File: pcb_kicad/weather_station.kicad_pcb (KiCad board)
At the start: 0 parts

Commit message: added full pcb schematic
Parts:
- added BT1: Battery_Cell, Battery:BatteryHolder_Keystone_1042_1x18650, F.Cu at (95.0, 105.1)
- added C1: 22u, Capacitor_SMD:C_0603_1608Metric_Pad1.08x0.95mm_HandSolder, F.Cu at (111.0, 98.5)
- added C10: 100n, Capacitor_SMD:C_0603_1608Metric_Pad1.08x0.95mm_HandSolder, F.Cu at (163.1, 83.0)
- added C2: 10u, Capacitor_SMD:C_0603_1608Metric_Pad1.08x0.95mm_HandSolder, F.Cu at (125.0, 102.0)
- added C3: 100n, Capacitor_SMD:C_0603_1608Metric_Pad1.08x0.95mm_HandSolder, F.Cu at (124.1, 105.5)
- added C4: 22u, Capacitor_SMD:C_0603_1608Metric_Pad1.08x0.95mm_HandSolder, F.Cu at (113.0, 98.5)
- added C5: 100nf, Capacitor_SMD:C_0603_1608Metric_Pad1.08x0.95mm_HandSolder, F.Cu at (116.0, 94.9)
- added C7: 10u, Capacitor_SMD:C_0603_1608Metric_Pad1.08x0.95mm_HandSolder, F.Cu at (111.0, 94.9)
- added C8: 0.1uF, Capacitor_SMD:C_0603_1608Metric_Pad1.08x0.95mm_HandSolder, F.Cu at (129.0, 93.5)
- added C9: 100n, Capacitor_SMD:C_0603_1608Metric_Pad1.08x0.95mm_HandSolder, F.Cu at (158.5, 83.0)
- added D1: LED, LED_SMD:LED_0603_1608Metric_Pad1.05x0.95mm_HandSolder, F.Cu at (116.0, 105.9)
- added J1: USB_C_Receptacle_PowerOnly_6P, Connector_USB:USB_C_Receptacle_GCT_USB4125-xx-x-0190_6P_TopMnt_Horizontal, F.Cu at (133.0, 107.0)
- added J2: Conn_02x05_Odd_Even, Connector_IDC:IDC-Header_2x05_P2.54mm_Vertical, F.Cu at (113.5, 66.5)
- added J3: Conn_02x03_Odd_Even, Connector_IDC:IDC-Header_2x03_P2.54mm_Vertical, F.Cu at (162.0, 71.5)
- added J4: Conn_01x06_Pin, Connector_PinHeader_2.54mm:PinHeader_1x06_P2.54mm_Vertical, F.Cu at (164.0, 105.0)
- added J5: Conn_01x02_Pin, TestPoint:TestPoint_2Pads_Pitch2.54mm_Drill0.8mm, F.Cu at (151.0, 71.8)
- added R1: 1000, Resistor_SMD:R_0603_1608Metric_Pad0.98x0.95mm_HandSolder, F.Cu at (163.1, 79.0)
- added R2: 500, Resistor_SMD:R_0603_1608Metric_Pad0.98x0.95mm_HandSolder, F.Cu at (118.5, 106.0)
- added R3: 1000, Resistor_SMD:R_0603_1608Metric_Pad0.98x0.95mm_HandSolder, F.Cu at (161.9, 96.0)
- added R4: 0R, Resistor_SMD:R_0603_1608Metric_Pad0.98x0.95mm_HandSolder, F.Cu at (120.5, 93.5)
- added R5: 0R, Resistor_SMD:R_0603_1608Metric_Pad0.98x0.95mm_HandSolder, F.Cu at (136.5, 100.0)
- added R6: 10k, Resistor_SMD:R_0603_1608Metric_Pad0.98x0.95mm_HandSolder, F.Cu at (124.5, 93.5)
- added R7: 0R, Resistor_SMD:R_0603_1608Metric_Pad0.98x0.95mm_HandSolder, F.Cu at (126.5, 98.5)
- added R8: 5.1k, Resistor_SMD:R_0603_1608Metric_Pad0.98x0.95mm_HandSolder, F.Cu at (133.5, 98.5)
- added R9: 5.1k, Resistor_SMD:R_0603_1608Metric_Pad0.98x0.95mm_HandSolder, F.Cu at (130.5, 98.5)
- added U2: BMP280, Package_LGA:Bosch_LGA-8_2.5x2.5mm_P0.65mm_ClockwisePinNumbering, F.Cu at (158.5, 79.5)
- added U3: AM2302, Sensor:ASAIR_AM2302_P2.54mm_Vertical, F.Cu at (145.5, 92.5)
- added U4: ADP5063, Package_DFN_QFN:QFN-20-1EP_4x4mm_P0.5mm_EP2.5x2.5mm, F.Cu at (118.1, 101.0)
- added U5: ESP32-WROOM-32, RF_Module:ESP32-WROOM-32D, F.Cu at (138.8, 69.5)
- added U6: LD1117S33TR_SOT223, Package_TO_SOT_SMD:SOT-223-3_TabPin2, F.Cu at (113.5, 88.0)
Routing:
- net GND: track 0.00 -> 319.6 mm
- net +3.3V: track 0.00 -> 210.1 mm, vias 0 -> 2
- net Net-(BT1-+): track 0.00 -> 125.4 mm, vias 0 -> 3
- net Net-(J3-Pin_1): track 0.00 -> 113.9 mm, vias 0 -> 2
- net Net-(J4-Pin_3): track 0.00 -> 50.0 mm, vias 0 -> 1
- net Net-(J4-Pin_4): track 0.00 -> 47.7 mm, vias 0 -> 1
- net Earth: track 0.00 -> 46.0 mm, vias 0 -> 2
- net Net-(U4-D_IO1): track 0.00 -> 37.6 mm
- net Net-(J2-Pin_6): track 0.00 -> 32.8 mm
- net Net-(U3-SDA): track 0.00 -> 27.2 mm
- net Net-(J2-Pin_8): track 0.00 -> 25.5 mm
- net Net-(J2-Pin_4): track 0.00 -> 24.5 mm
- net Net-(J1-VBUS-PadA9): track 0.00 -> 20.7 mm
- net Net-(J2-Pin_2): track 0.00 -> 18.1 mm
- net Net-(J3-Pin_3): track 0.00 -> 17.4 mm, vias 0 -> 1
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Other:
- board outline added: 85 x 91 mm
- copper layers 0 -> 2

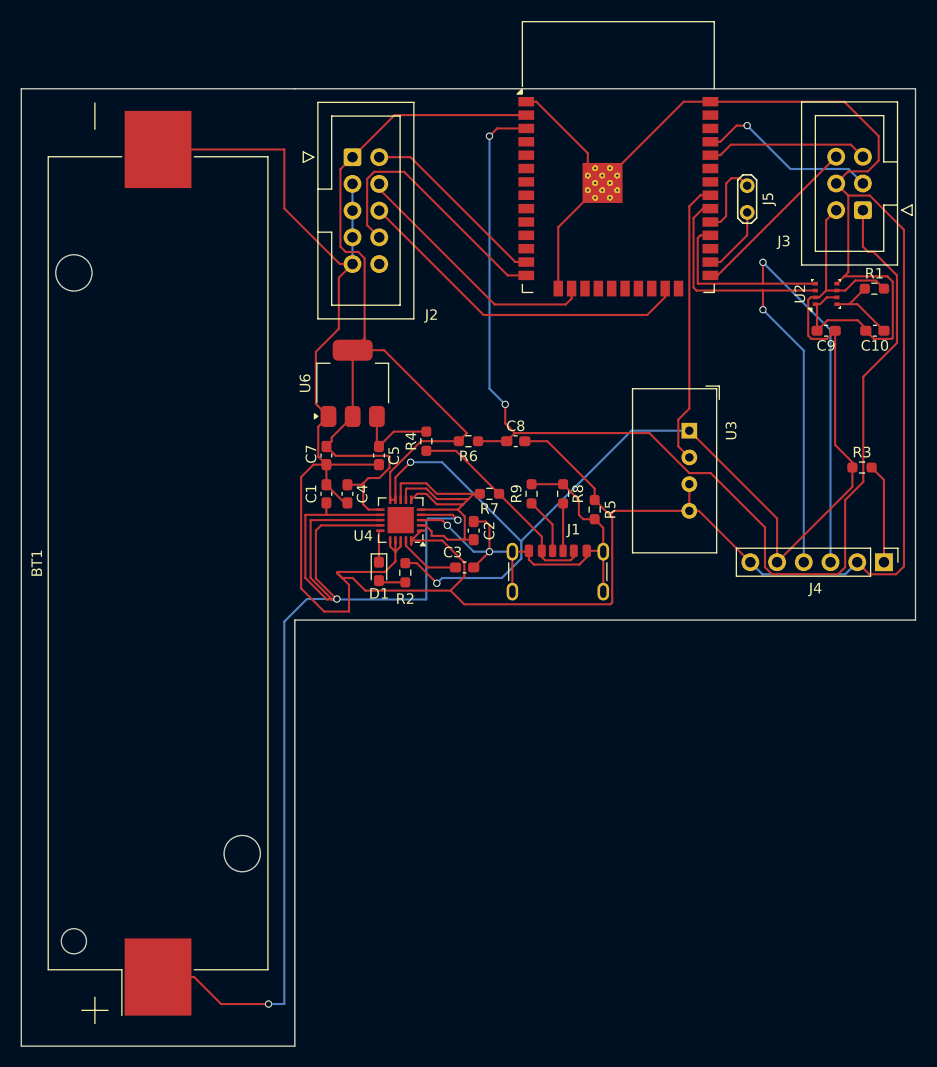
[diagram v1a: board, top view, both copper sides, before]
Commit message: added ground fills
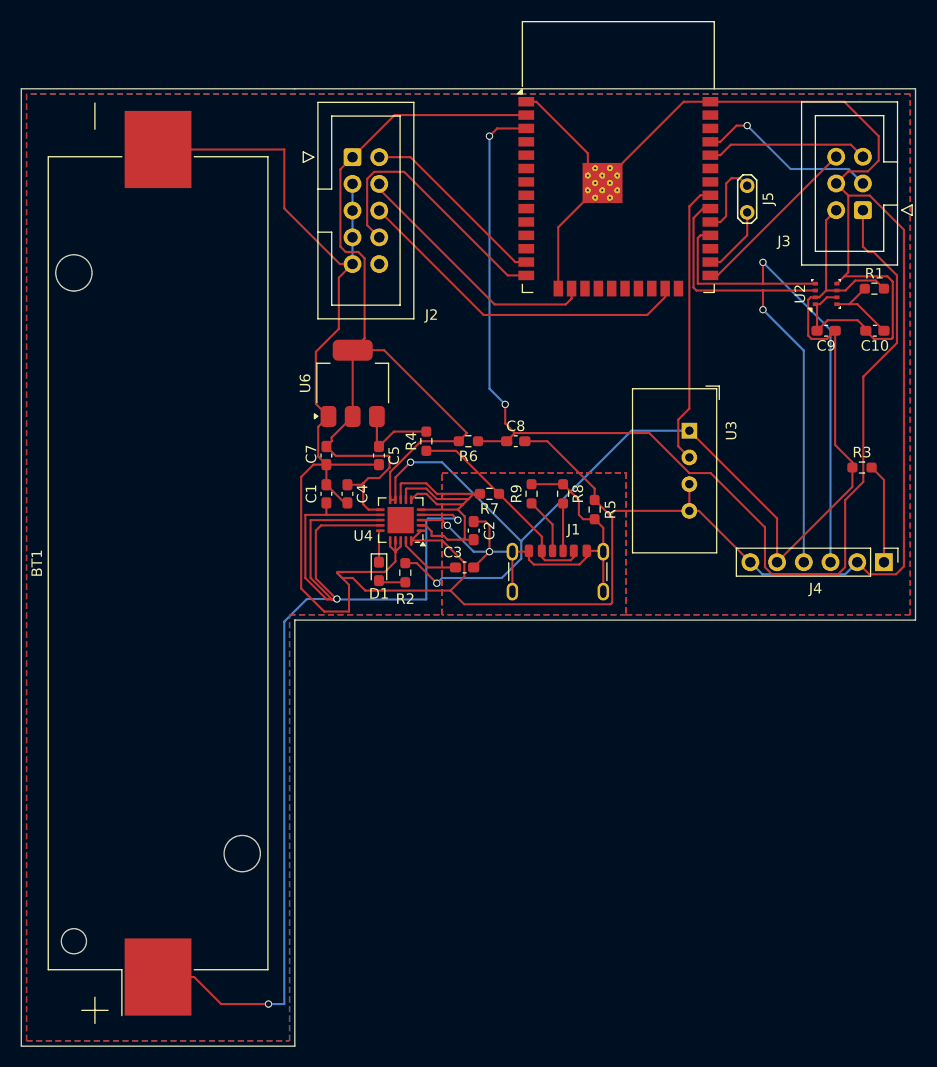
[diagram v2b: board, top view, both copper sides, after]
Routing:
- added copper zone on B.Cu, net Earth
- added copper zone on B.Cu, net GND
- added copper zone on F.Cu, net GND
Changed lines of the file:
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@@
 		(tags "resistor handsolder")
 		(property "Reference" "R4"
-			(at 0 -1.43 270)
+			(at 0 -1.43 -90)
 			(layer "F.SilkS")
 			(effects
@@
 		)
 		(property "Value" "0R"
-			(at 0 1.43 270)
+			(at 0 1.43 -90)
 			(layer "F.Fab")
 			(effects
@@
 		)
 		(fp_text user "${REFERENCE}"
-			(at 0 0 270)
+			(at 0 0 -90)
 			(layer "F.Fab")
 			(effects
@@
 		(tags "capacitor handsolder")
 		(property "Reference" "C3"
-			(at -1.1375 -1.43 360)
+			(at -1.1375 -1.43 0)
 			(layer "F.SilkS")
 			(effects
@@
 		)
 		(property "Value" "100n"
-			(at 0 1.43 360)
+			(at 0 1.43 0)
 			(layer "F.Fab")
 			(effects
@@
 		)
 		(fp_text user "${REFERENCE}"
-			(at 0 0 360)
+			(at 0 0 0)
 			(layer "F.Fab")
 			(effects
@@
 		(tags "Through hole vertical IDC box header THT 2x05 2.54mm double row")
 		(property "Reference" "J2"
-			(at 7.516346 15 360)
+			(at 7.516346 15 0)
 			(layer "F.SilkS")
 			(effects
@@
 		)
 		(property "Value" "Conn_02x05_Odd_Even"
-			(at 1.27 16.26 360)
+			(at 1.27 16.26 0)
 			(layer "F.Fab")
 			(hide yes)
@@
 		)
 		(property "Value" "500"
-			(at 0 1.43 270)
+			(at 0 1.43 -90)
 			(layer "F.Fab")
 			(effects
@@
 		)
 		(fp_text user "${REFERENCE}"
-			(at 0 0 270)
+			(at 0 0 -90)
 			(layer "F.Fab")
 			(effects
@@
 		(tags "CONN DEV")
 		(property "Reference" "J5"
-			(at 1.3 2 270)
+			(at 1.3 2 -90)
 			(layer "F.SilkS")
 			(effects
@@
 		)
 		(property "Value" "Conn_01x02_Pin"
-			(at 1.27 2 270)
+			(at 1.27 2 -90)
 			(layer "F.Fab")
 			(effects
@@
 		)
 		(fp_text user "${REFERENCE}"
-			(at 1.3 -2 270)
+			(at 1.3 -2 -90)
 			(layer "F.Fab")
 			(effects
@@
 		(tags "capacitor handsolder")
 		(property "Reference" "C7"
-			(at 0.1375 -1.43 270)
+			(at 0.1375 -1.43 -90)
 			(layer "F.SilkS")
 			(effects
@@
 		)
 		(property "Value" "10u"
-			(at 0 1.43 270)
+			(at 0 1.43 -90)
 			(layer "F.Fab")
 			(effects
@@
 		)
 		(fp_text user "${REFERENCE}"
-			(at 0 0 270)
+			(at 0 0 -90)
 			(layer "F.Fab")
 			(effects
@@
 		(tags "capacitor handsolder")
 		(property "Reference" "C2"
-			(at 0 1.5 270)
+			(at 0 1.5 -90)
 			(layer "F.SilkS")
 			(effects
@@
 		)
 		(property "Value" "10u"
-			(at 0 1.43 270)
+			(at 0 1.43 -90)
 			(layer "F.Fab")
 			(effects
@@
 		)
 		(fp_text user "${REFERENCE}"
-			(at 0 0 270)
+			(at 0 0 -90)
 			(layer "F.Fab")
 			(effects
@@
 		(tags "capacitor handsolder")
 		(property "Reference" "C1"
-			(at 0 -1.43 270)
+			(at 0 -1.43 -90)
 			(layer "F.SilkS")
 			(effects
@@
 		)
 		(property "Value" "22u"
-			(at 0 1.43 270)
+			(at 0 1.43 -90)
 			(layer "F.Fab")
 			(effects
@@
 		)
 		(fp_text user "${REFERENCE}"
-			(at 0 0 270)
+			(at 0 0 -90)
 			(layer "F.Fab")
 			(effects
@@
 		(tags "capacitor handsolder")
 		(property "Reference" "C8"
-			(at 0 -1.43 360)
+			(at 0 -1.43 0)
 			(layer "F.SilkS")
 			(effects
@@
 		)
 		(property "Value" "0.1uF"
-			(at 0 1.43 360)
+			(at 0 1.43 0)
 			(layer "F.Fab")
 			(effects
@@
 		)
 		(fp_text user "${REFERENCE}"
-			(at 0 0 360)
+			(at 0 0 0)
 			(layer "F.Fab")
 			(effects
@@
 		(tags "CMS SOT")
 		(property "Reference" "U6"
-			(at 0 -4.5 270)
+			(at 0 -4.5 -90)
 			(layer "F.SilkS")
 			(effects
@@
 		)
 		(property "Value" "LD1117S33TR_SOT223"
-			(at -0.16 5.483654 270)
+			(at -0.16 5.483654 -90)
 			(layer "F.Fab")
 			(effects
@@
 		)
 		(fp_text user "${REFERENCE}"
-			(at 0 0 360)
+			(at 0 0 0)
 			(layer "F.Fab")
 			(effects
@@
 		(tags "18650 Keystone 1042 Li-ion")
 		(property "Reference" "BT1"
-			(at 0 -11.5 270)
+			(at 0 -11.5 -90)
 			(layer "F.SilkS")
 			(effects
@@
 		)
 		(property "Value" "Battery_Cell"
-			(at 0 11.3 270)
+			(at 0 11.3 -90)
 			(layer "F.Fab")
 			(effects
@@
 		)
 		(fp_text user "${REFERENCE}"
-			(at 0 0 270)
+			(at 0 0 -90)
 			(layer "F.Fab")
 			(effects
@@
 		(tags "lga land grid array")
 		(property "Reference" "U2"
-			(at 0.015 -2.465 270)
+			(at 0.015 -2.465 -90)
 			(layer "F.SilkS")
 			(effects
@@
 		)
 		(property "Value" "BMP280"
-			(at 0.015 2.535 270)
+			(at 0.015 2.535 -90)
 			(layer "F.Fab")
 			(effects
@@
 		)
 		(fp_text user "${REFERENCE}"
-			(at 0 0 270)
+			(at 0 0 -90)
 			(layer "F.Fab")
 			(effects
@@
 		(tags "resistor handsolder")
 		(property "Reference" "R3"
-			(at 0 -1.43 360)
+			(at 0 -1.43 0)
 			(layer "F.SilkS")
 			(effects
@@
 		)
 		(property "Value" "1000"
-			(at 0 1.43 360)
+			(at 0 1.43 0)
 			(layer "F.Fab")
 			(effects
@@
 		)
 		(fp_text user "${REFERENCE}"
-			(at 0 0 360)
+			(at 0 0 0)
 			(layer "F.Fab")
 			(effects
@@
 		(tags "resistor handsolder")
 		(property "Reference" "R9"
-			(at 0 -1.43 270)
+			(at 0 -1.43 -90)
 			(layer "F.SilkS")
 			(effects
@@
 		)
 		(property "Value" "5.1k"
-			(at 0 1.43 270)
+			(at 0 1.43 -90)
 			(layer "F.Fab")
 			(effects
@@
 		)
 		(fp_text user "${REFERENCE}"
-			(at 0 0 270)
+			(at 0 0 -90)
 			(layer "F.Fab")
 			(effects
@@
 		)
 		(fp_text user "${REFERENCE}"
-			(at 1.27 2.54 270)
+			(at 1.27 2.54 -90)
 			(layer "F.Fab")
 			(effects
@@
 		(net 50)
 	)
+	(zone
+		(net 2)
+		(net_name "GND")
+		(layer "F.Cu")
+		(hatch edge 0.5)
+		(priority 2)
+		(connect_pads
+			(clearance 0.5)
+		)
+		(min_thickness 0.25)
+		(filled_areas_thickness no)
+		(fill yes
+			(thermal_gap 0.5)
+			(thermal_bridge_width 0.5)
+		)
+		(polygon
+			(pts
+				(xy 139.5 110) (xy 122 110) (xy 122 96.5) (xy 139.5 96.5)
+			)
+		)
+	)
+	(zone
+		(net 2)
+		(net_name "GND")
+		(layers "F&B.Cu")
+		(hatch edge 0.5)
+		(connect_pads
+			(clearance 0.5)
+		)
+		(min_thickness 0.25)
+		(filled_areas_thickness no)
+		(fill yes
+			(thermal_gap 0.5)
+			(thermal_bridge_width 0.5)
+		)
+		(polygon
+			(pts
+				(xy 166.5 110) (xy 166.5 60.5) (xy 82.5 60.5) (xy 82.5 150.5) (xy 107.5 150.5) (xy 107.5 110) (xy 122 110)
+				(xy 122 96.5) (xy 139.5 96.5) (xy 139.5 110)
+			)
+		)
+	)
+	(zone
+		(net 4)
+		(net_name "Earth")
+		(layer "B.Cu")
+		(hatch edge 0.5)
+		(priority 1)
+		(connect_pads
+			(clearance 0.5)
+		)
+		(min_thickness 0.25)
+		(filled_areas_thickness no)
+		(fill yes
+			(thermal_gap 0.5)
+			(thermal_bridge_width 0.5)
+		)
+		(polygon
+			(pts
+				(xy 139.5 110) (xy 122 110) (xy 122 96.5) (xy 139.5 96.5)
+			)
+		)
+	)
 )

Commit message: added 0 ohm resistors for battery only mode, out pins for all unused pins from esp 32, opened blind vias and removed unsupported vias and silkscreen drawings from esp32 blueprint
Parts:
- added J6: Conn_01x11_Pin, Connector_PinHeader_2.54mm:PinHeader_1x11_P2.54mm_Vertical, F.Cu at (149.7, 86.0)
- added J7: Conn_01x01_Pin, Connector_PinSocket_2.54mm:PinSocket_1x01_P2.54mm_Vertical, F.Cu at (143.5, 82.0)
- added R10: 0R, Resistor_SMD:R_0603_1608Metric_Pad0.98x0.95mm_HandSolder, F.Cu at (102.6, 148.5)
- added R11: 0R, Resistor_SMD:R_0603_1608Metric_Pad0.98x0.95mm_HandSolder, F.Cu at (103.4, 147.0)
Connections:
- C1 pad 1: Net-(BT1-+) -> Net-(U4-BAT_SNS)
- U4 pad 12: Net-(BT1-+) -> Net-(U4-BAT_SNS)
- U4 pad 13: Net-(BT1-+) -> Net-(U4-BAT_SNS)
- U4 pad 14: Net-(BT1-+) -> Net-(U4-BAT_SNS)
- U4 pad 4: Net-(BT1-+) -> Net-(U4-BAT_SNS)
- U5 pad 10: unconnected-(U5-IO25-Pad10) -> Net-(J6-Pin_5)
- U5 pad 11: unconnected-(U5-IO26-Pad11) -> Net-(J6-Pin_6)
- U5 pad 12: unconnected-(U5-IO27-Pad12) -> Net-(J6-Pin_7)
- U5 pad 24: unconnected-(U5-IO2-Pad24) -> Net-(J7-Pin_1)
- U5 pad 27: unconnected-(U5-IO16-Pad27) -> Net-(J6-Pin_1)
- U5 pad 33: unconnected-(U5-IO21-Pad33) -> Net-(J6-Pin_2)
- U5 pad 36: unconnected-(U5-IO22-Pad36) -> Net-(J6-Pin_3)
- U5 pad 37: unconnected-(U5-IO23-Pad37) -> Net-(J6-Pin_4)
- U5 pad 6: unconnected-(U5-IO34-Pad6) -> Net-(J6-Pin_10)
- U5 pad 7: unconnected-(U5-IO35-Pad7) -> Net-(J6-Pin_11)
- U5 pad 8: unconnected-(U5-IO32-Pad8) -> Net-(J6-Pin_8)
- U5 pad 9: unconnected-(U5-IO33-Pad9) -> Net-(J6-Pin_9)
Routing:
- net Net-(U4-BAT_SNS): track 0.00 -> 116.0 mm, vias 0 -> 3
- net Net-(BT1-+): track 125.4 -> 10.3 mm, vias 3 -> 0
- net +3.3V: track 210.1 -> 277.1 mm, vias 2 -> 3
- net Net-(J6-Pin_9): track 0.00 -> 41.7 mm, vias 0 -> 1
- net Net-(J6-Pin_11): track 0.00 -> 31.8 mm, vias 0 -> 1
- net Net-(J6-Pin_3): track 0.00 -> 30.2 mm, vias 0 -> 1
- net Net-(J6-Pin_4): track 0.00 -> 29.0 mm, vias 0 -> 1
- net Net-(J6-Pin_5): track 0.00 -> 27.2 mm, vias 0 -> 1
- net Net-(J6-Pin_6): track 0.00 -> 23.9 mm, vias 0 -> 1
- net Net-(J6-Pin_2): track 0.00 -> 22.2 mm, vias 0 -> 1
- net Net-(J6-Pin_10): track 0.00 -> 20.7 mm, vias 0 -> 1
- net Net-(J6-Pin_7): track 0.00 -> 20.7 mm, vias 0 -> 1
- net Net-(J6-Pin_8): track 0.00 -> 20.2 mm, vias 0 -> 1
- net Net-(J6-Pin_1): track 0.00 -> 14.6 mm, vias 0 -> 1
- net Net-(U3-SDA): track 27.2 -> 34.7 mm
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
